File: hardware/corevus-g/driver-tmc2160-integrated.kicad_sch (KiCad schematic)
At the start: 34 parts, among them M5 Micro-Fit 3.0, Q1 30N06, Q2 30N06, Q3 30N06, Q4 30N06, Q5 30N06, Q6 30N06, Q7 30N06, Q8 30N06, U1 TMC2160

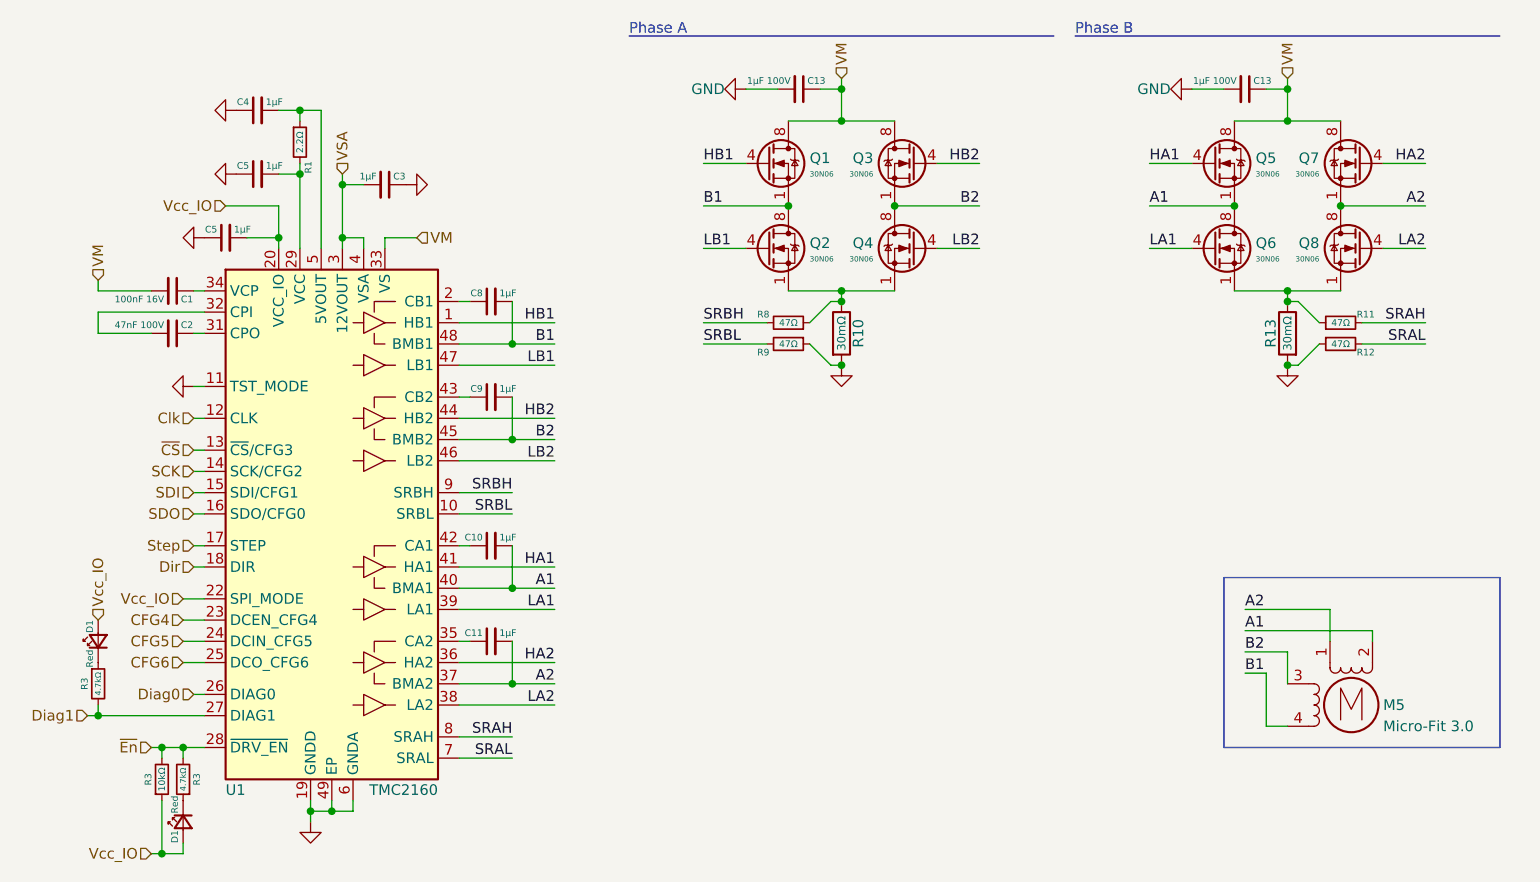
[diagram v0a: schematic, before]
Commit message: version control appears to have magically disappeared the single and dual 2160 driver files :(((((((((, but got some work done on CvG nonetheless
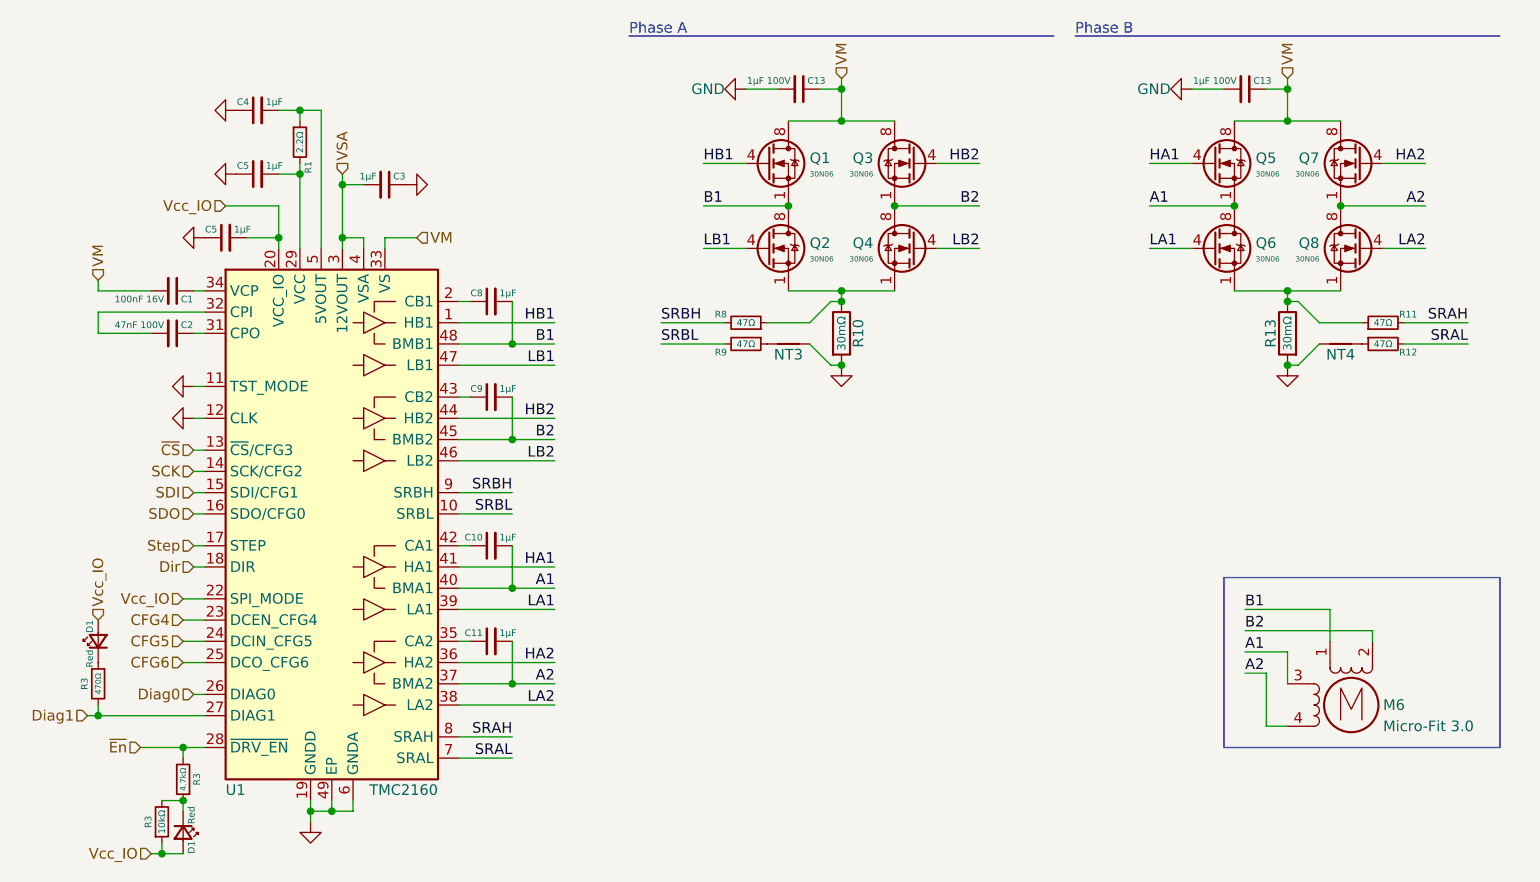
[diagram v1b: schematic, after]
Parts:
- added NT3, NT4: NetTie_2, corevus:NetTie-2_SMD_Pad0.1mm, symbol Device:NetTie_2
- M6: renamed from M5; footprint corevus:JST_XH_1x04-Side -> corevus:XKB_X3025WR-04
- R3: value 4.7kΩ -> 470Ω
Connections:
- net Clk is gone; now on net GND: U1.12 (CLK)
- net A1: now also M6.3; no longer M6.2 (-)
- net A2: now also M6.4; no longer M6.1
- net B1: now also M6.1; no longer M6.4
- net B2: now also M6.2 (-); no longer M6.3
- net GND: now also NT3.2, NT4.1; no longer R12.1, R9.1
- net ~{En}: no longer R3.2
- net at D1.1 (K), R3.1: now also R3.2
- new net: NT4.2, R12.1
- new net: NT3.1, R9.1
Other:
- moved on the sheet: D1, R11, R12, R3, R8, R9

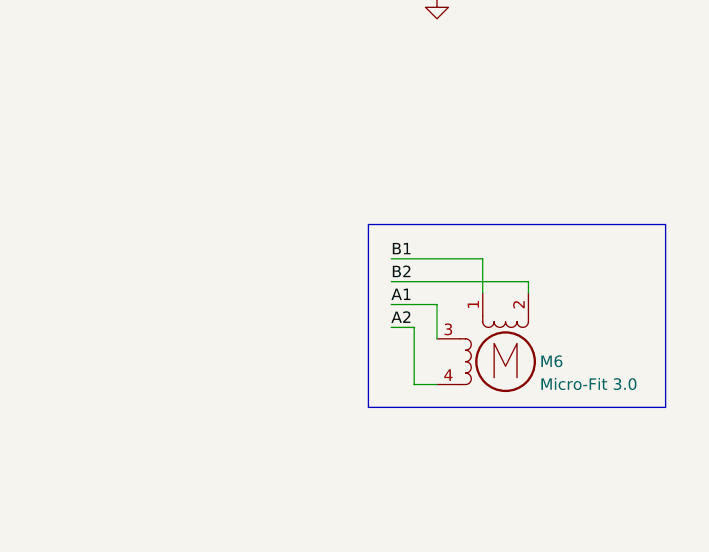
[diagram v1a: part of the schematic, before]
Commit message: v0.4 mostly complete, board needs minor revisions (e.g. pin swap)
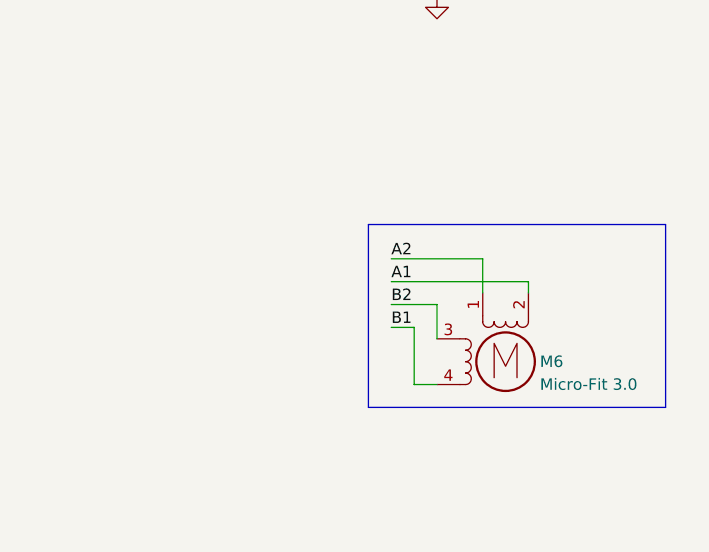
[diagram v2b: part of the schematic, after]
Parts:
- M6: footprint corevus:XKB_X3025WR-04 -> corevus:JST_XH_1x04
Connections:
- net A1: now also M6.2 (-); no longer M6.3
- net A2: now also M6.1; no longer M6.4
- net B1: now also M6.4; no longer M6.1
- net B2: now also M6.3; no longer M6.2 (-)
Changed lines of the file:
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@@
     (effects (font (size 1.27 1.27)) (justify right bottom))
   )
-  (label "A1" (at 163.83 88.9 0) (fields_autoplaced)
+  (label "A1" (at 163.83 86.36 0) (fields_autoplaced)
     (effects (font (size 1.27 1.27)) (justify left bottom))
   )
@@
     (effects (font (size 1.27 1.27)) (justify left bottom))
   )
-  (label "A2" (at 163.83 91.44 0) (fields_autoplaced)
+  (label "A2" (at 163.83 83.82 0) (fields_autoplaced)
     (effects (font (size 1.27 1.27)) (justify left bottom))
   )
@@
     (effects (font (size 1.27 1.27)) (justify right bottom))
   )
-  (label "B1" (at 163.83 83.82 0) (fields_autoplaced)
+  (label "B1" (at 163.83 91.44 0) (fields_autoplaced)
     (effects (font (size 1.27 1.27)) (justify left bottom))
   )
@@
     (effects (font (size 1.27 1.27)) (justify right bottom))
   )
-  (label "B2" (at 163.83 86.36 0) (fields_autoplaced)
+  (label "B2" (at 163.83 88.9 0) (fields_autoplaced)
     (effects (font (size 1.27 1.27)) (justify left bottom))
   )
@@
       )
       (project "corevus-g"
-        (path "/1a565782-f217-442e-b118-196625f31c53"
-          (reference "R?") (unit 1)
-        )
         (path "/1a565782-f217-442e-b118-196625f31c53/d34aeff3-da22-4edc-92e0-1591d6117dbc"
           (reference "R107") (unit 1)
@@
       )
       (project "corevus-g"
-        (path "/1a565782-f217-442e-b118-196625f31c53"
-          (reference "R?") (unit 1)
-        )
         (path "/1a565782-f217-442e-b118-196625f31c53/d34aeff3-da22-4edc-92e0-1591d6117dbc"
           (reference "R119") (unit 1)
@@
       )
       (project "corevus-g"
-        (path "/1a565782-f217-442e-b118-196625f31c53"
-          (reference "R?") (unit 1)
-        )
         (path "/1a565782-f217-442e-b118-196625f31c53/d34aeff3-da22-4edc-92e0-1591d6117dbc"
           (reference "R99") (unit 1)
@@
       )
       (project "corevus-g"
-        (path "/1a565782-f217-442e-b118-196625f31c53"
-          (reference "D?") (unit 1)
-        )
         (path "/1a565782-f217-442e-b118-196625f31c53/d34aeff3-da22-4edc-92e0-1591d6117dbc"
           (reference "D13") (unit 1)
@@
       (effects (font (size 1.27 1.27)) (justify left))
     )
-    (property "Footprint" "corevus:XKB_X3025WR-04" (at 176.784 95.504 0)
+    (property "Footprint" "corevus:JST_XH_1x04" (at 176.784 95.504 0)
       (effects (font (size 1.27 1.27)) hide)
     )
@@
       )
       (project "corevus-g"
-        (path "/1a565782-f217-442e-b118-196625f31c53"
-          (reference "D?") (unit 1)
-        )
         (path "/1a565782-f217-442e-b118-196625f31c53/d34aeff3-da22-4edc-92e0-1591d6117dbc"
           (reference "D20") (unit 1)

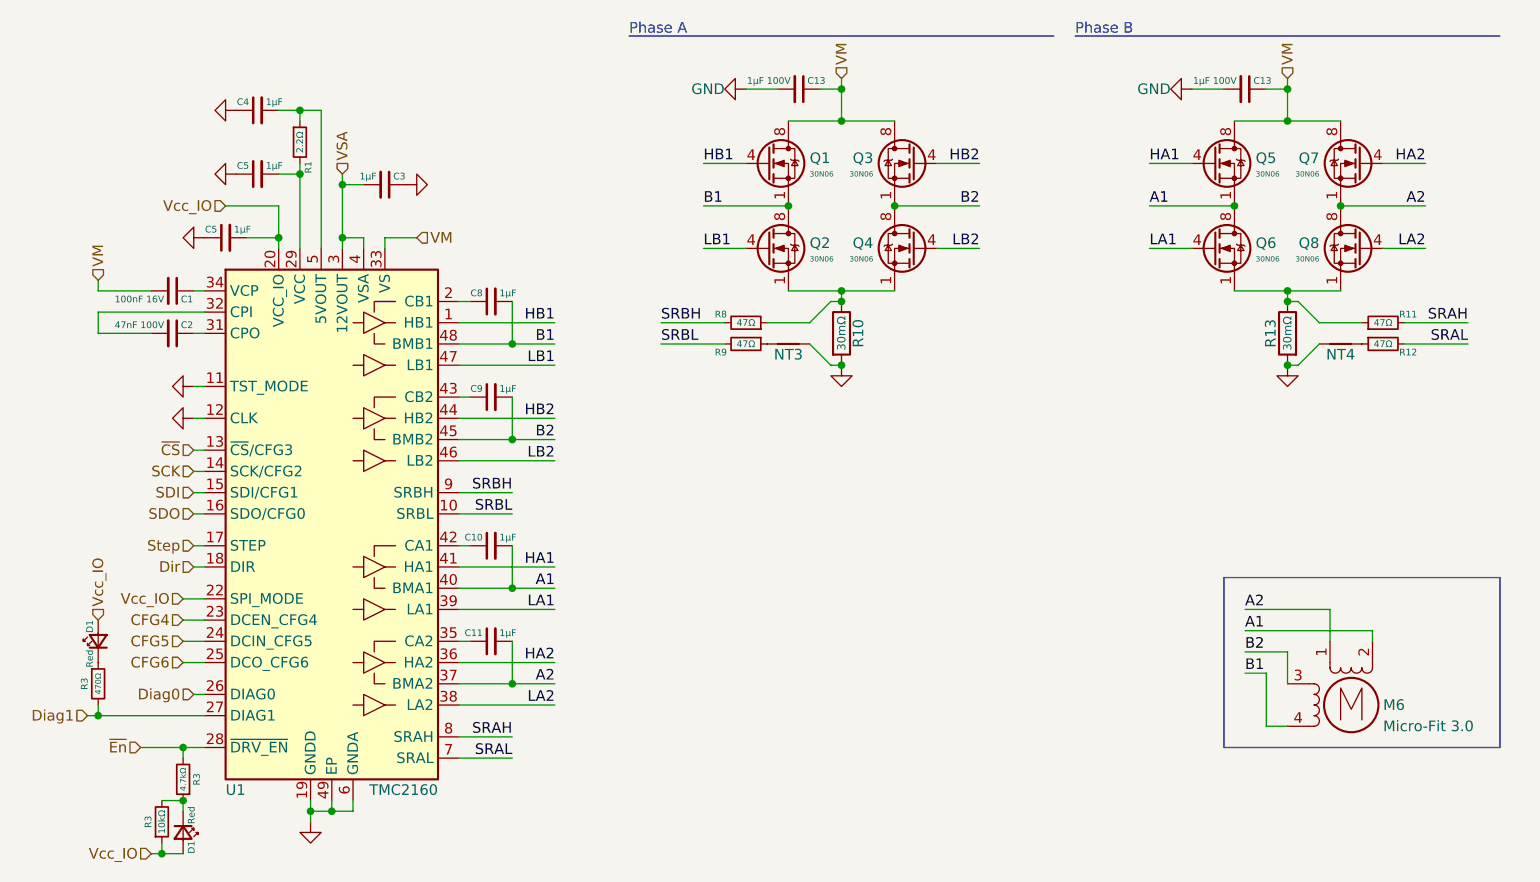
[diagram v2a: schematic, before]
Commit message: corevus toolboard v0.2 release (working), corevus-g v0.2 release (very much not working), m++ v0.1 (not working, needs a lot of bodges)
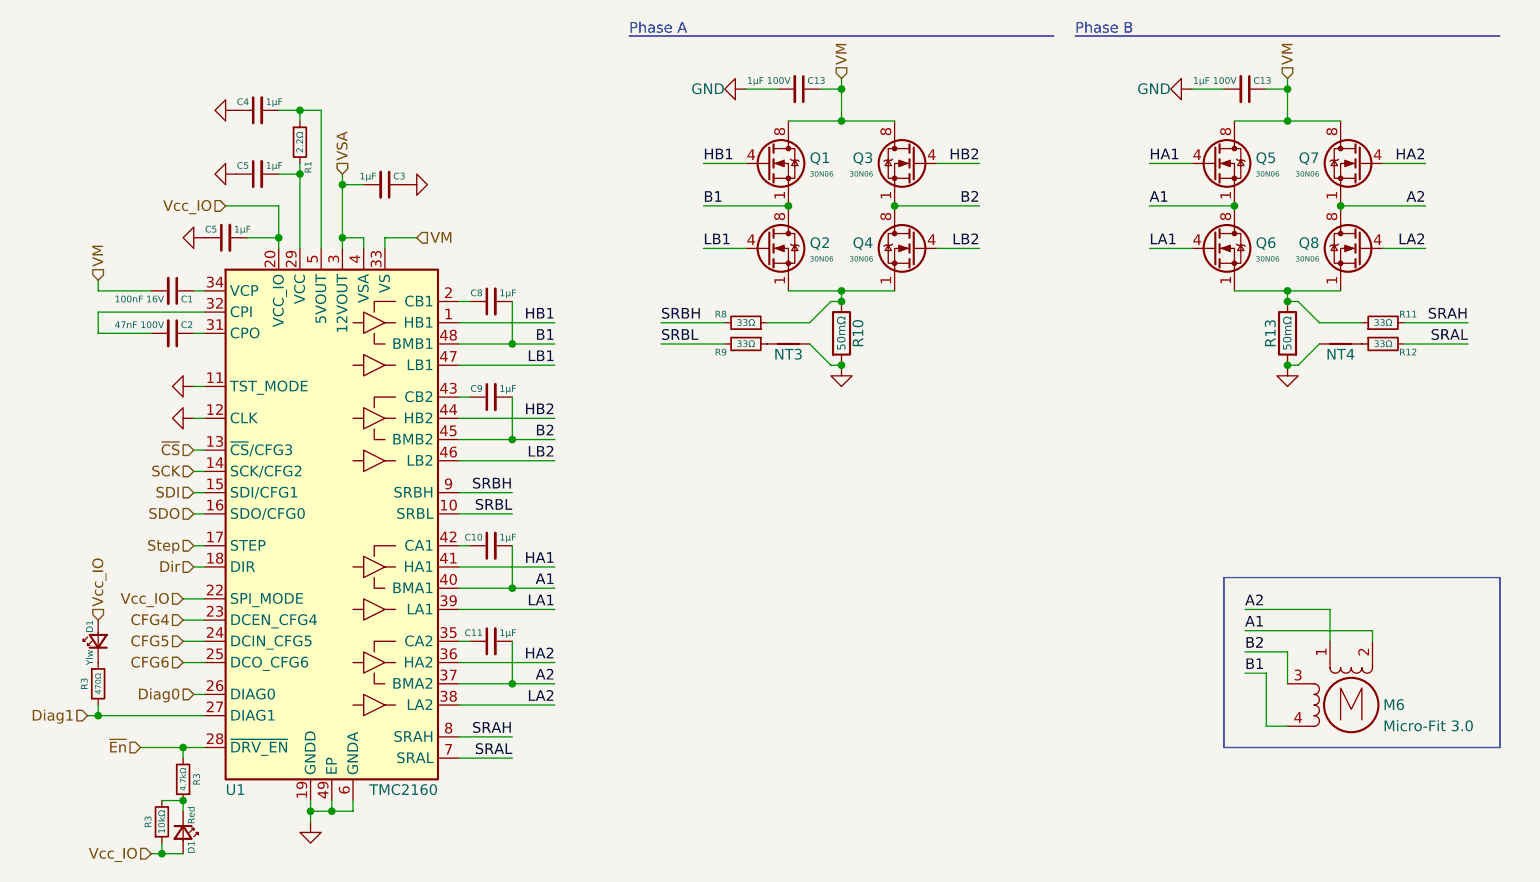
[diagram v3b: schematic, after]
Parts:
- D1: value Red -> Ylw
- R10, R13: value 30mΩ -> 50mΩ
- R11, R12, R8, R9: value 47Ω -> 33Ω

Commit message: why not
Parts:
- D1: value Ylw -> Grn
- M6: value Micro-Fit 3.0 -> JST XH
- R1: value 2.2Ω -> 1Ω
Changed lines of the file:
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@@
 			)
 		)
-		(property "Value" "Ylw"
+		(property "Value" "Grn"
 			(at 25.67 88.63 0)
 			(effects
@@
 			)
 		)
-		(property "Value" "Micro-Fit 3.0"
+		(property "Value" "JST XH"
 			(at 180.34 97.79 0)
 			(effects
@@
 			)
 		)
-		(property "Value" "2.2Ω"
+		(property "Value" "1Ω"
 			(at 50.8 27.94 90)
 			(effects

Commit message: should be up to date for cvg v0.6 and latest protected drivers
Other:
- moved on the sheet: C4, C5
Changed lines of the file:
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@@
 	(wire
 		(pts
-			(xy 48.26 24.13) (xy 50.8 24.13)
+			(xy 49.53 24.13) (xy 50.8 24.13)
 		)
 		(stroke
@@
 	(wire
 		(pts
-			(xy 48.26 31.75) (xy 50.8 31.75)
+			(xy 49.53 31.75) (xy 50.8 31.75)
 		)
 		(stroke
@@
 	(symbol
 		(lib_id "power:GND")
-		(at 43.18 24.13 270)
+		(at 44.45 24.13 270)
 		(unit 1)
 		(exclude_from_sim no)
@@
 		(fields_autoplaced yes)
 		(property "Reference" "#PWR02"
-			(at 36.83 24.13 0)
+			(at 38.1 24.13 0)
 			(effects
 				(font
@@
 		)
 		(property "Value" "GND"
-			(at 38.1 24.13 0)
+			(at 39.37 24.13 0)
 			(effects
 				(font
@@
 		)
 		(property "Footprint" ""
-			(at 43.18 24.13 0)
+			(at 44.45 24.13 0)
 			(effects
 				(font
@@
 		)
 		(property "Datasheet" ""
-			(at 43.18 24.13 0)
+			(at 44.45 24.13 0)
 			(effects
 				(font
@@
 		)
 		(property "Description" ""
-			(at 43.18 24.13 0)
+			(at 44.45 24.13 0)
 			(effects
 				(font
@@
 	(symbol
 		(lib_id "Device:C_Small")
-		(at 45.72 24.13 90)
+		(at 46.99 24.13 90)
 		(mirror x)
 		(unit 1)
@@
 		(dnp no)
 		(property "Reference" "C4"
-			(at 44.72 23.13 90)
+			(at 45.99 23.13 90)
 			(effects
 				(font
@@
 		)
 		(property "Value" "1μF"
-			(at 46.72 23.13 90)
+			(at 47.99 23.13 90)
 			(effects
 				(font
@@
 		)
 		(property "Footprint" "AlphaLib:0402C"
-			(at 45.72 24.13 0)
+			(at 46.99 24.13 0)
 			(effects
 				(font
@@
 		)
 		(property "Datasheet" "~"
-			(at 45.72 24.13 0)
+			(at 46.99 24.13 0)
 			(effects
 				(font
@@
 		)
 		(property "Description" ""
-			(at 45.72 24.13 0)
+			(at 46.99 24.13 0)
 			(effects
 				(font
@@
 	(symbol
 		(lib_id "Device:C_Small")
-		(at 45.72 31.75 90)
+		(at 46.99 31.75 90)
 		(mirror x)
 		(unit 1)
@@
 		(dnp no)
 		(property "Reference" "C5"
-			(at 44.72 30.75 90)
+			(at 45.99 30.75 90)
 			(effects
 				(font
@@
 		)
 		(property "Value" "1μF"
-			(at 46.72 30.75 90)
+			(at 47.99 30.75 90)
 			(effects
 				(font
@@
 		)
 		(property "Footprint" "AlphaLib:0402C"
-			(at 45.72 31.75 0)
+			(at 46.99 31.75 0)
 			(effects
 				(font
@@
 		)
 		(property "Datasheet" "~"
-			(at 45.72 31.75 0)
+			(at 46.99 31.75 0)
 			(effects
 				(font
@@
 		)
 		(property "Description" ""
-			(at 45.72 31.75 0)
+			(at 46.99 31.75 0)
 			(effects
 				(font
@@
 	(symbol
 		(lib_id "power:GND")
-		(at 43.18 31.75 270)
+		(at 44.45 31.75 270)
 		(unit 1)
 		(exclude_from_sim no)
@@
 		(fields_autoplaced yes)
 		(property "Reference" "#PWR02"
-			(at 36.83 31.75 0)
+			(at 38.1 31.75 0)
 			(effects
 				(font
@@
 		)
 		(property "Value" "GND"
-			(at 38.1 31.75 0)
+			(at 39.37 31.75 0)
 			(effects
 				(font
@@
 		)
 		(property "Footprint" ""
-			(at 43.18 31.75 0)
+			(at 44.45 31.75 0)
 			(effects
 				(font
@@
 		)
 		(property "Datasheet" ""
-			(at 43.18 31.75 0)
+			(at 44.45 31.75 0)
 			(effects
 				(font
@@
 		)
 		(property "Description" ""
-			(at 43.18 31.75 0)
+			(at 44.45 31.75 0)
 			(effects
 				(font
